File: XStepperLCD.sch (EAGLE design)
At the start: 28 parts, among them Q2 16 MHZ, U1 LCD-16X2NOHOLES

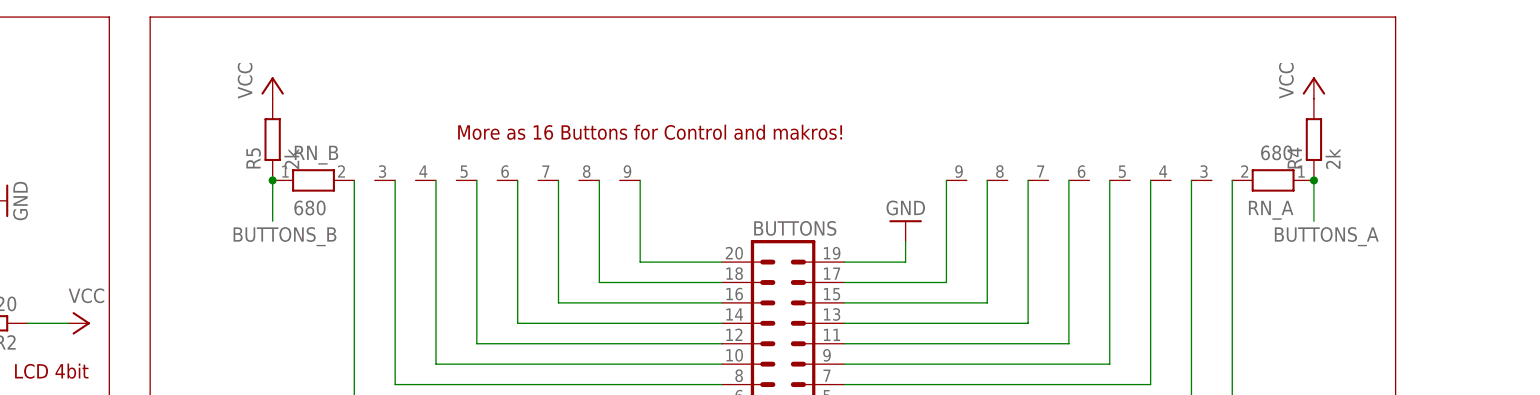
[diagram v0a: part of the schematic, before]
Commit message: - damn, misstake with branches work on master
- add a lot changes for LCDMenu
- use phi_interfaces for analog buttons
- remove a lot unused code
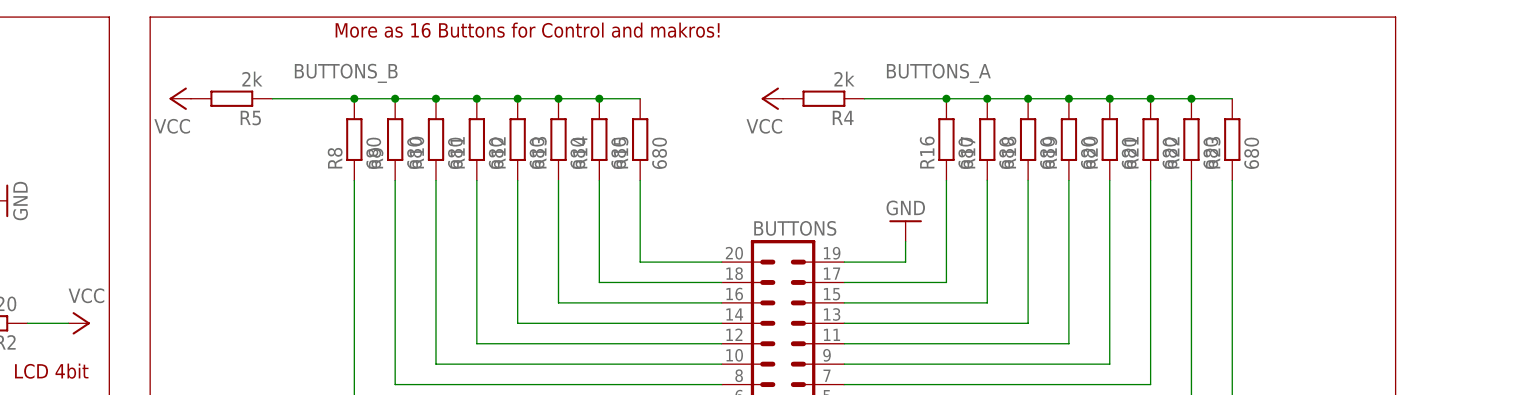
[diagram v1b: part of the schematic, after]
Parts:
- removed RN_A, RN_B: 680, resistor-net:RN08
- added R10, R11, R12, R13, R14, R15, R16, R17, R18, R19, R20, R21, R22, R23, R8, R9: 680, resistor:R-EU_R1206
- C1, C13: device resistor:C-EU025-025X050 -> resistor:C-EUC1206
- C12: device resistor:C-EU025-025X050 -> resistor:C-EUC1206K
- R2, R3, R4, R5, R6, R7: device resistor:R-EU_0204/7 -> resistor:R-EU_R1206
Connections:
- net BUTTONS_A: now also R16.2, R17.2, R18.2, R19.2, R20.2, R21.2, R22.2, R23.2; no longer RN_A.1
- net BUTTONS_B: now also R10.2, R11.2, R12.2, R13.2, R14.2, R15.2, R8.2, R9.2; no longer RN_B.1
- net N$10: now also R22.1; no longer RN_A.3
- net N$11: now also R10.1; no longer RN_B.4
- net N$12: now also R11.1; no longer RN_B.5
- net N$13: now also R12.1; no longer RN_B.6
- net N$15: now also R13.1; no longer RN_B.7
- net N$16: now also R21.1; no longer RN_A.4
- net N$17: now also R20.1; no longer RN_A.5
- net N$18: now also R19.1; no longer RN_A.6
- net N$19: now also R14.1; no longer RN_B.8
- net N$20: now also R15.1; no longer RN_B.9
- net N$4: now also R18.1; no longer RN_A.7
- net N$5: now also R17.1; no longer RN_A.8
- net N$6: now also R16.1; no longer RN_A.9
- net N$7: now also R8.1; no longer RN_B.2
- net N$8: now also R9.1; no longer RN_B.3
- net N$9: now also R23.1; no longer RN_A.2
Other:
- moved on the sheet: R4, R5
